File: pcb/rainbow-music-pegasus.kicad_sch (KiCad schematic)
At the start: 88 parts, among them J1 USB_B_Micro, J2 Conn_02x03_Odd_Even, SW1 SW_SPDT, U1 ESP32-C3-MINI-1, U2 OPA344NA, U3 TLV75533PDBV

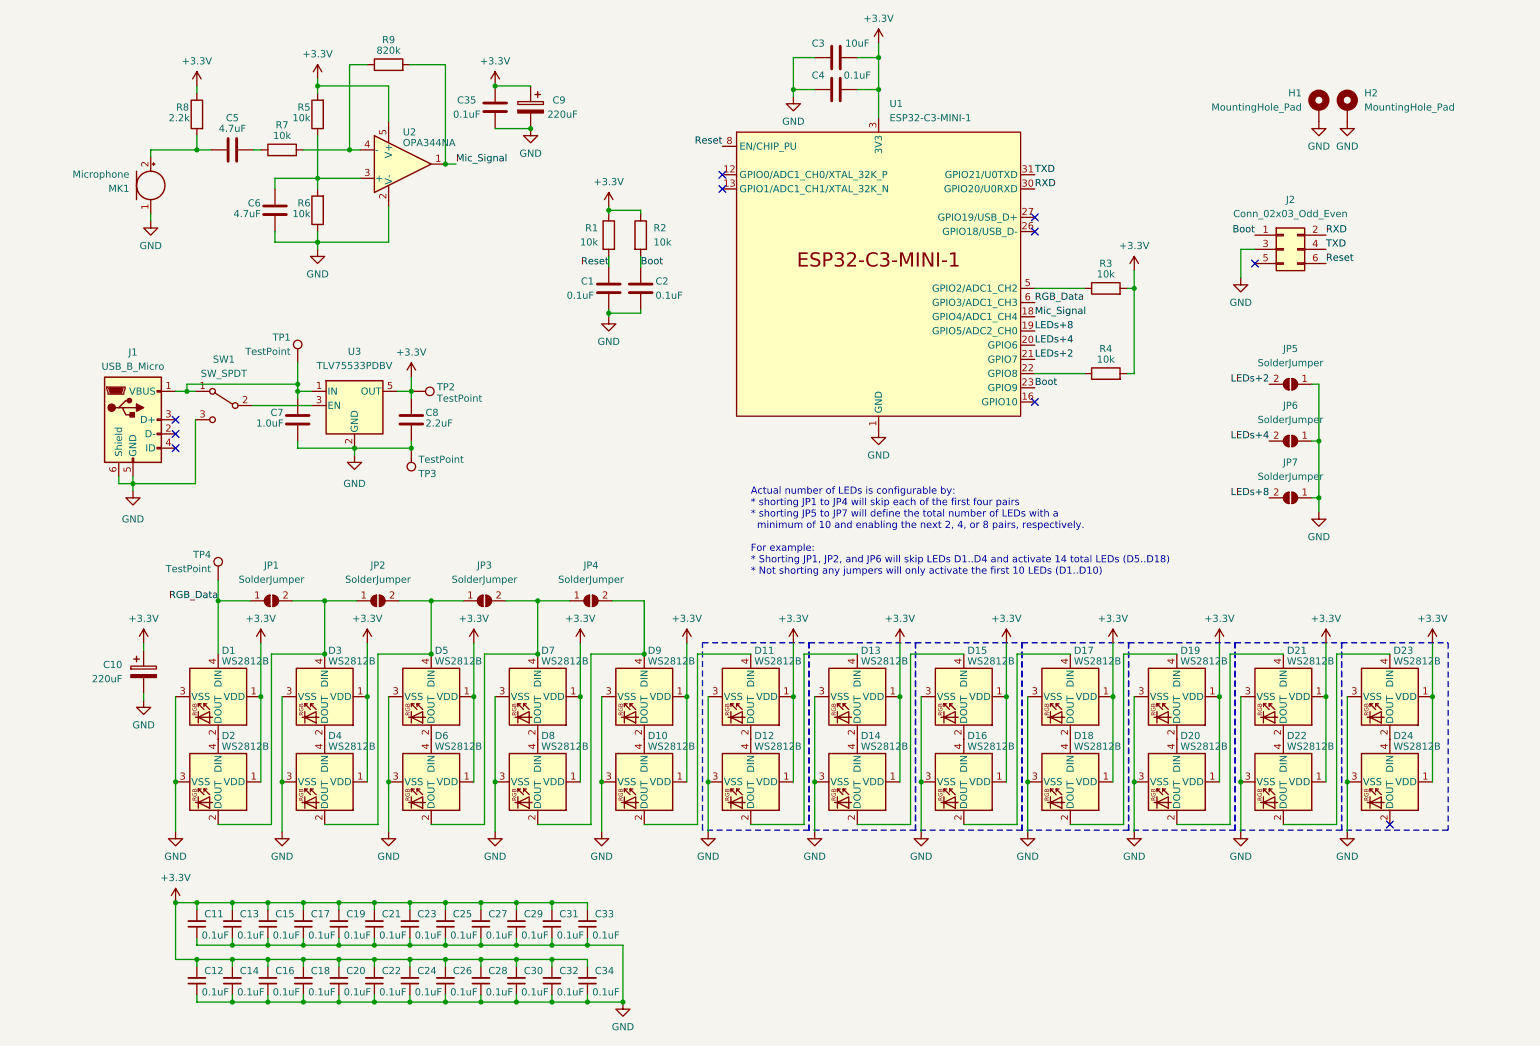
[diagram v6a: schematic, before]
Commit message: Added Battery charging module and a new mode-setting button
Also found 3d models for the microphone, switch, USB components
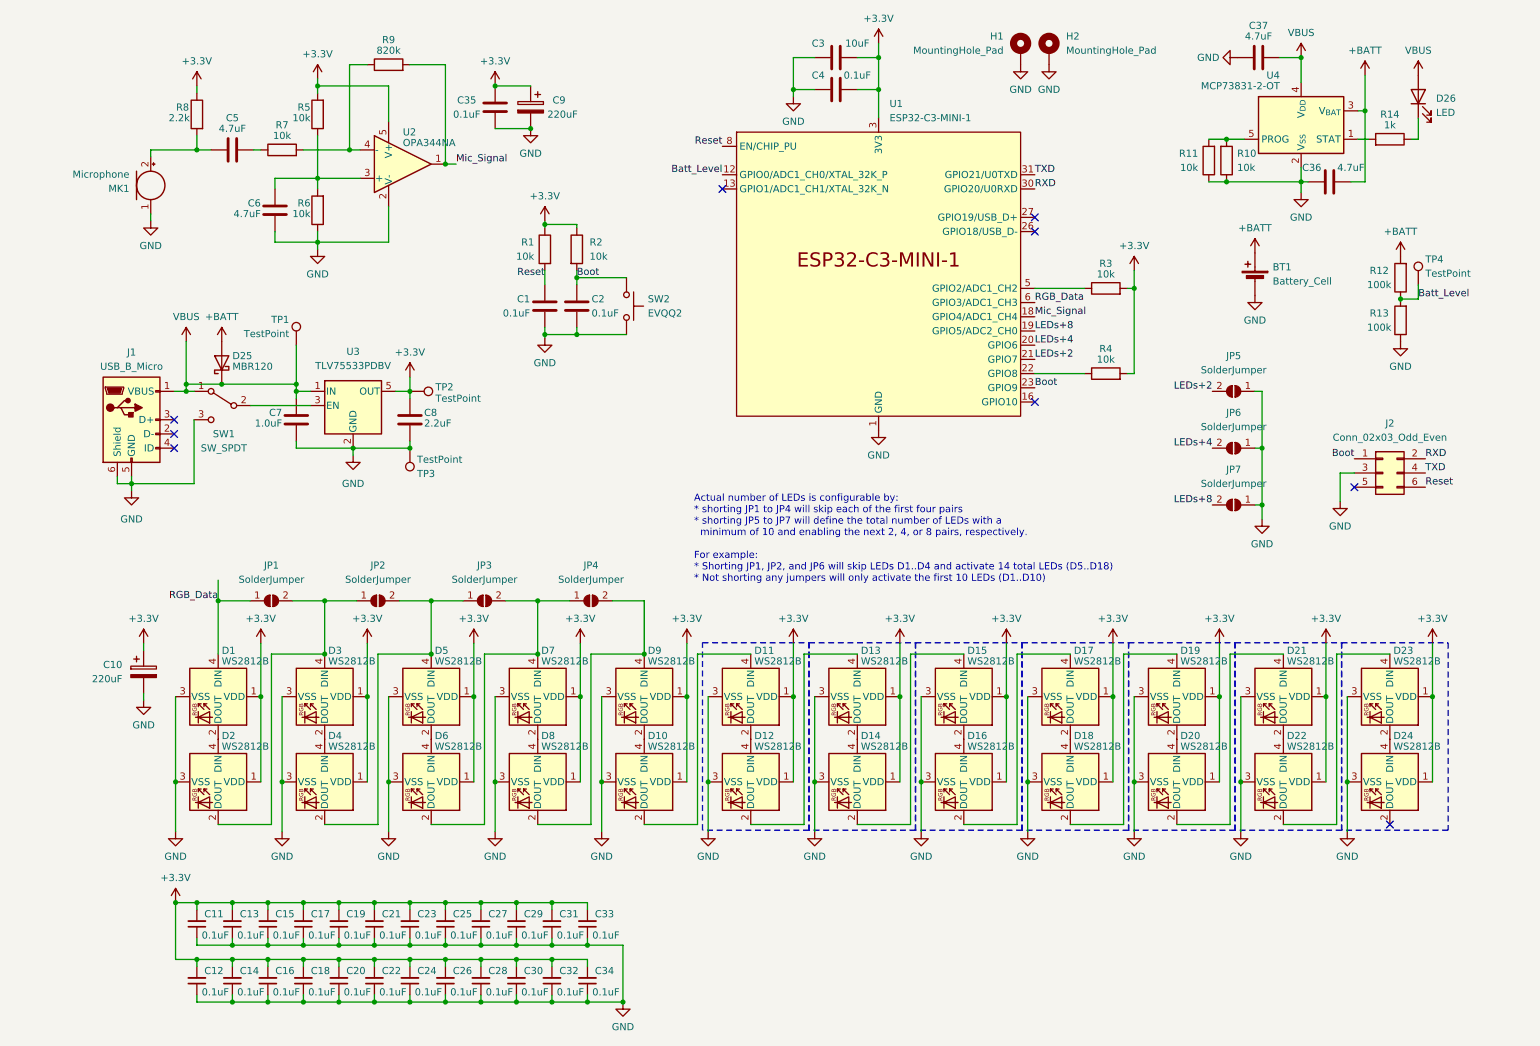
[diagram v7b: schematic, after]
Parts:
- added BT1: Battery_Cell, Connector_JST:JST_PH_B2B-PH-K_1x02_P2.00mm_Vertical, symbol Device:Battery_Cell
- added C36, C37: 4.7uF, Capacitor_SMD:C_0805_2012Metric, symbol Device:C
- added D25: MBR120, Diode_SMD:D_SOD-123, symbol Diode:MBR0520
- added D26: LED, LED_SMD:LED_0603_1608Metric, symbol Device:LED
- added R10, R11: 10k, Resistor_SMD:R_0805_2012Metric, symbol Device:R
- added R12, R13: 100k, Resistor_SMD:R_0805_2012Metric, symbol Device:R
- added R14: 1k, Resistor_SMD:R_0805_2012Metric, symbol Device:R
- added SW2: EVQQ2, Button_Switch_SMD:SW_SPST_EVQQ2, symbol Switch:SW_Push
- added U4: MCP73831-2-OT, Package_TO_SOT_SMD:SOT-23-5, symbol Battery_Management:MCP73831-2-OT
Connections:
- net Boot: now also SW2.1
- net GND: now also BT1.2 (-), C36.1, C37.1, R10.1, R11.1, R13.1, SW2.2, U4.2 (V_{SS})
- net RGB_Data: no longer TP4.1
- net VBUS: now reaches C7.2, J1.1 (VBUS), SW1.1 (A), TP1.1, U3.1 (IN)
- net VBUS: now also C37.2, D25.1 (K), D26.2 (A), U4.4 (V_{DD})
- net Batt_Level: now reaches U1.12 (GPIO0/ADC1_CH0/XTAL_32K_P)
- net Batt_Level: now also TP4.1, R12.1, R13.2
- new net: D26.1 (K), R14.1
- new net: R14.2, U4.1 (STAT)
- new net: R10.2, R11.2, U4.5 (PROG)
- new net +BATT: BT1.1 (+), C36.2, D25.2 (A), R12.2, U4.3 (V_{BAT})
- no-connect marks 10 -> 9
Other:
- moved on the sheet: C1, C2, H1, H2, J2, JP5, JP6, JP7, R1, R2, TP1, TP4

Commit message: Finalized battery design including charging status lights
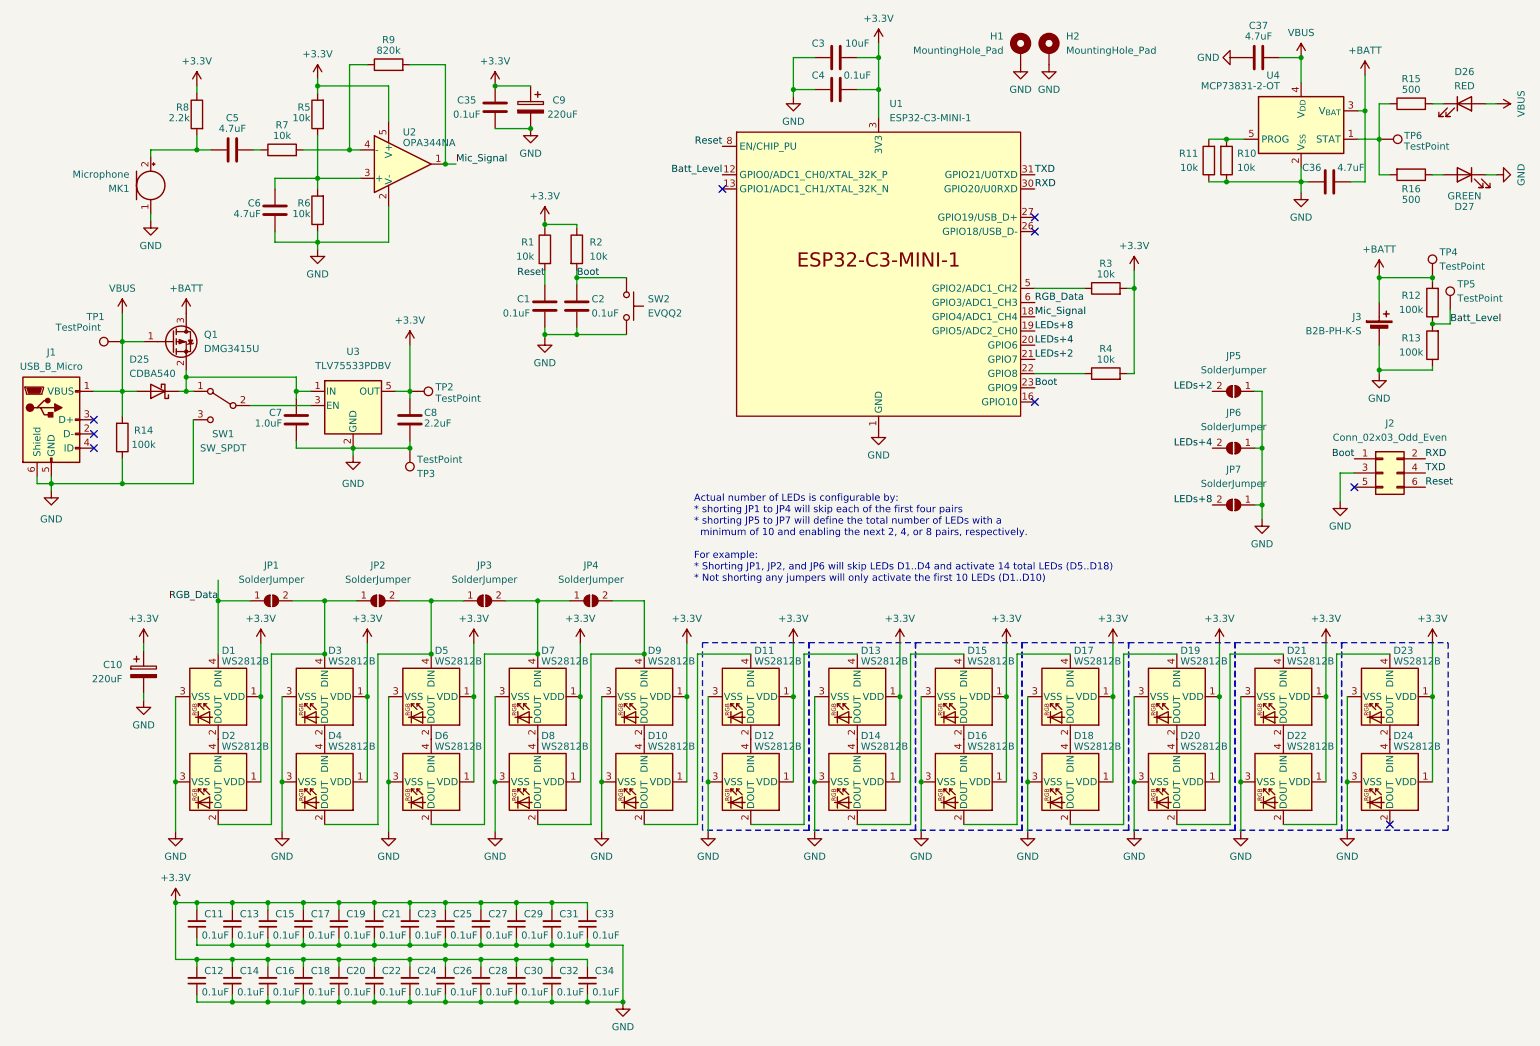
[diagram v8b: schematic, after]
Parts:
- added D27: GREEN, LED_SMD:LED_0603_1608Metric, symbol Device:LED
- added Q1: DMG3415U, Package_TO_SOT_SMD:SOT-23, symbol Transistor_FET:DMG2301L
- added R14: 100k, Resistor_SMD:R_0805_2012Metric, symbol Device:R
- added R15: 500, Resistor_SMD:R_0603_1608Metric, symbol Device:R
- added TP5, TP6: TestPoint, TestPoint:TestPoint_THTPad_1.5x1.5mm_Drill0.7mm, symbol Connector:TestPoint
- D25: value MBR120 -> CDBA540; footprint Diode_SMD:D_SOD-123 -> Diode_SMD:D_SMA
- D26: value LED -> RED
- J3: renamed from BT1; value Battery_Cell -> B2B-PH-K-S
- R16: renamed from R14; value 1k -> 500; footprint Resistor_SMD:R_0805_2012Metric -> Resistor_SMD:R_0603_1608Metric
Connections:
- net +BATT: now also TP4.1, Q1.3 (D); no longer D25.2 (A)
- net Batt_Level: now also TP5.1; no longer TP4.1
- net GND: now also D27.1 (K), R14.1
- net VBUS: now also D25.2 (A), Q1.1 (G), R14.2; no longer C7.2, D25.1 (K), SW1.1 (A), U3.1 (IN)
- net at R16.1: now also D27.2 (A); no longer D26.1 (K)
- net at R16.2, U4.1 (STAT): now also R15.1, TP6.1
- new net: C7.2, D25.1 (K), Q1.2 (S), SW1.1 (A), U3.1 (IN)
- new net: D26.1 (K), R15.2
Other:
- moved on the sheet: D25, D26, J1, J3, R12, R13, R16, TP1, TP4
